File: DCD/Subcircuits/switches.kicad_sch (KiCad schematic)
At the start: 0 parts

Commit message: Did the signal switching, finished ADC, misc changes to top
Decided to go with solder jumpers instead of power switches bc power
switches have no specs of linearity and they would add unnecessary
complexity, development time, and routing problems.

The calibration test has to be done only once and the chamber doesn't
even have to be sealed for it, so it shouldn't add too much hassle.
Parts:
- added C3: 1nF, Capacitor_SMD:C_0603_1608Metric, symbol Device:C_Small
- added JP1, JP2, JP3, JP4, JP9: SolderJumper_3_Bridged12, Jumper:SolderJumper-3_P1.3mm_Bridged12_RoundedPad1.0x1.5mm, symbol Jumper:SolderJumper_3_Bridged12
- added R2, R3, R4, R5, R6, R7: 47, Resistor_SMD:R_0603_1608Metric, symbol Device:R
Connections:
- new net: JP4.1 (A), R6.2, R7.2
- new net: JP1.2 (C), JP4.2 (C)
- new net: JP4.3 (B), R3.2, R4.2
- new net: JP1.1 (A), JP9.1 (A)
- new net: C3.1, JP1.3 (B), R2.1
- new net: JP3.1 (A), JP9.2 (C)
- new net: JP9.3 (B), R2.2
- new net: JP2.1 (A), JP3.2 (C)
- new net: JP3.3 (B), R5.1
- new net ADC1: R4.1
- new net ADC2: R6.1
- new net DAC1: R3.1
- new net DAC2: R7.1
- new net Ext_Analog: JP2.2 (C)
- new net GND: C3.2, JP2.3 (B), R5.2

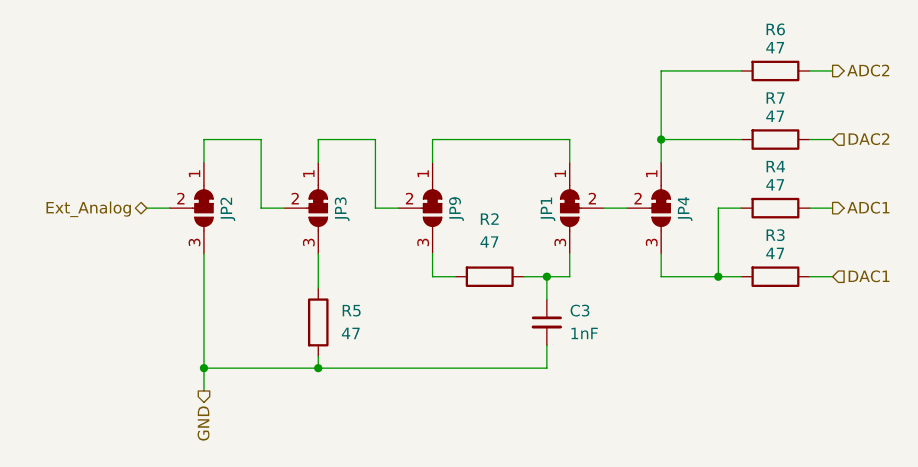
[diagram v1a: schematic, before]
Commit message: Finished switches, added calculations of the current consumption
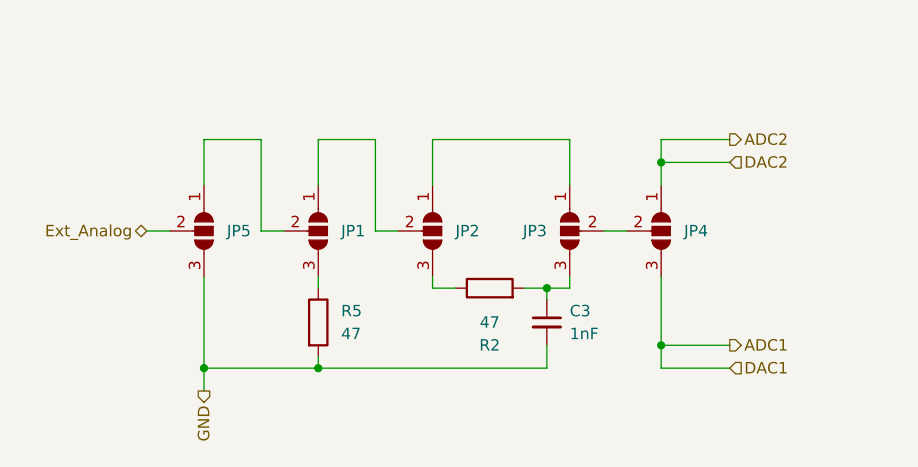
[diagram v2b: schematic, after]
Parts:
- removed JP1, JP2, JP3, JP4, JP9: SolderJumper_3_Bridged12, Jumper:SolderJumper-3_P1.3mm_Bridged12_RoundedPad1.0x1.5mm, symbol Jumper:SolderJumper_3_Bridged12
- removed R3, R4, R6, R7: 47, Resistor_SMD:R_0603_1608Metric, symbol Device:R
- added JP1, JP2, JP3, JP4, JP5: SolderJumper_3_Open, Jumper:SolderJumper-3_P1.3mm_Open_RoundedPad1.0x1.5mm, symbol Jumper:SolderJumper_3_Open
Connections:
- net ADC1: now also JP4.3 (B)
- net ADC2: now also JP4.1 (A)
- net Ext_Analog: now also JP5.2 (C)
- net GND: now also JP5.3 (B)
- net at R2.1: now also JP2.3 (B); no longer C3.1
- net at R2.2: now also C3.1, JP3.3 (B)
- net at R5.1: now also JP1.3 (B)
- new net: JP1.1 (A), JP2.2 (C)
- new net: JP1.2 (C), JP5.1 (A)
- new net: JP2.1 (A), JP3.1 (A)
- new net: JP3.2 (C), JP4.2 (C)
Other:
- moved on the sheet: R2

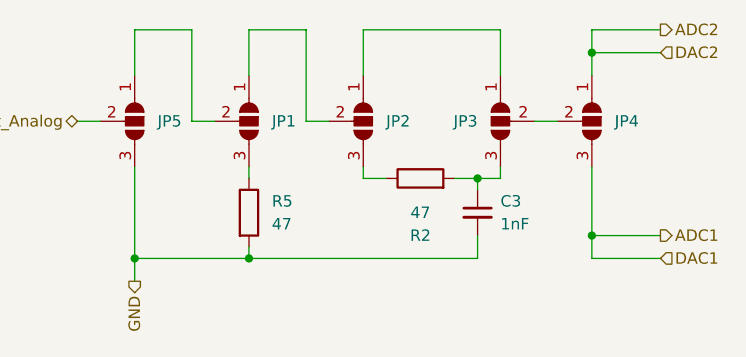
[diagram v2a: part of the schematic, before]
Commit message: Progress on the implementation of the DAC driver
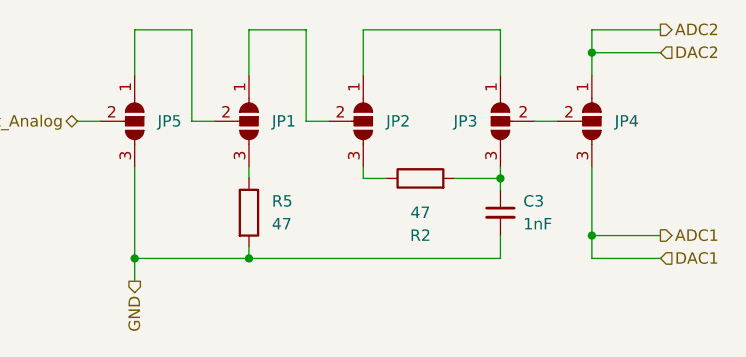
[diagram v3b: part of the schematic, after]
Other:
- moved on the sheet: C3
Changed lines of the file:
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@@
 	(paper "A5")
+	(junction
+		(at 101.6 73.66)
+		(diameter 0)
+		(color 0 0 0 0)
+	)
 	(junction
 		(at 111.76 59.69)
@@
 	)
 	(junction
-		(at 99.06 73.66)
-		(diameter 0)
-		(color 0 0 0 0)
-	)
-	(junction
 		(at 111.76 80.01)
 		(diameter 0)
@@
 	(wire
 		(pts
-			(xy 73.66 82.55) (xy 99.06 82.55)
+			(xy 73.66 82.55) (xy 101.6 82.55)
 		)
 		(stroke
@@
 	(wire
 		(pts
-			(xy 101.6 73.66) (xy 99.06 73.66)
-		)
-		(stroke
-			(width 0)
-			(type default)
-		)
-	)
-	(wire
-		(pts
 			(xy 80.01 57.15) (xy 80.01 67.31)
 		)
@@
 	(wire
 		(pts
-			(xy 99.06 74.93) (xy 99.06 73.66)
-		)
-		(stroke
-			(width 0)
-			(type default)
-		)
-	)
-	(wire
-		(pts
-			(xy 99.06 80.01) (xy 99.06 82.55)
+			(xy 101.6 74.93) (xy 101.6 73.66)
+		)
+		(stroke
+			(width 0)
+			(type default)
+		)
+	)
+	(wire
+		(pts
+			(xy 101.6 80.01) (xy 101.6 82.55)
 		)
 		(stroke
@@
 	(wire
 		(pts
-			(xy 99.06 73.66) (xy 96.52 73.66)
+			(xy 96.52 73.66) (xy 101.6 73.66)
 		)
 		(stroke
@@
 	(symbol
 		(lib_id "Device:C_Small")
-		(at 99.06 77.47 0)
+		(at 101.6 77.47 0)
 		(unit 1)
 		(exclude_from_sim no)
@@
 		(dnp no)
 		(property "Reference" "C3"
-			(at 101.6 76.2 0)
+			(at 104.14 76.2 0)
 			(effects
 				(font
@@
 		)
 		(property "Value" "1nF"
-			(at 101.6 78.74 0)
+			(at 104.14 78.74 0)
 			(effects
 				(font
@@
 		)
 		(property "Footprint" "Capacitor_SMD:C_0603_1608Metric"
-			(at 99.06 77.47 0)
+			(at 101.6 77.47 0)
 			(effects
 				(font
@@
 		)
 		(property "Datasheet" "https://datasheets.kyocera-avx.com/C0GNP0-KGM.pdf"
-			(at 99.06 77.47 0)
+			(at 101.6 77.47 0)
 			(effects
 				(font
@@
 		)
 		(property "Description" ""
-			(at 99.06 77.47 0)
+			(at 101.6 77.47 0)
 			(effects
 				(font
@@
 		)
 		(property "Part number" "0603YA102FAT2A "
-			(at 99.06 77.47 0)
+			(at 101.6 77.47 0)
 			(effects
 				(font
@@
 		)
 		(property "Order number" "581-0603YA102FAT2A"
-			(at 99.06 77.47 0)
+			(at 101.6 77.47 0)
 			(effects
 				(font
@@
 		)
 		(property "Supplier" "Mouser"
-			(at 99.06 77.47 0)
+			(at 101.6 77.47 0)
 			(effects
 				(font
@@
 		)
 		(property "Notes" ""
-			(at 99.06 77.47 0)
+			(at 101.6 77.47 0)
 			(effects
 				(font
@@
 		)
 		(property "Link" "https://www.mouser.com/ProductDetail/KYOCERA-AVX/0603YA102FAT2A?qs=Q0wCMCRSJ1vE1Ym6h4QWAA%3D%3D"
-			(at 99.06 77.47 0)
+			(at 101.6 77.47 0)
 			(effects
 				(font
@@
 		)
 		(property "Mouser No." ""
-			(at 99.06 77.47 0)
-			(effects
-				(font
+			(at 101.6 77.47 0)
+			(effects
+				(font

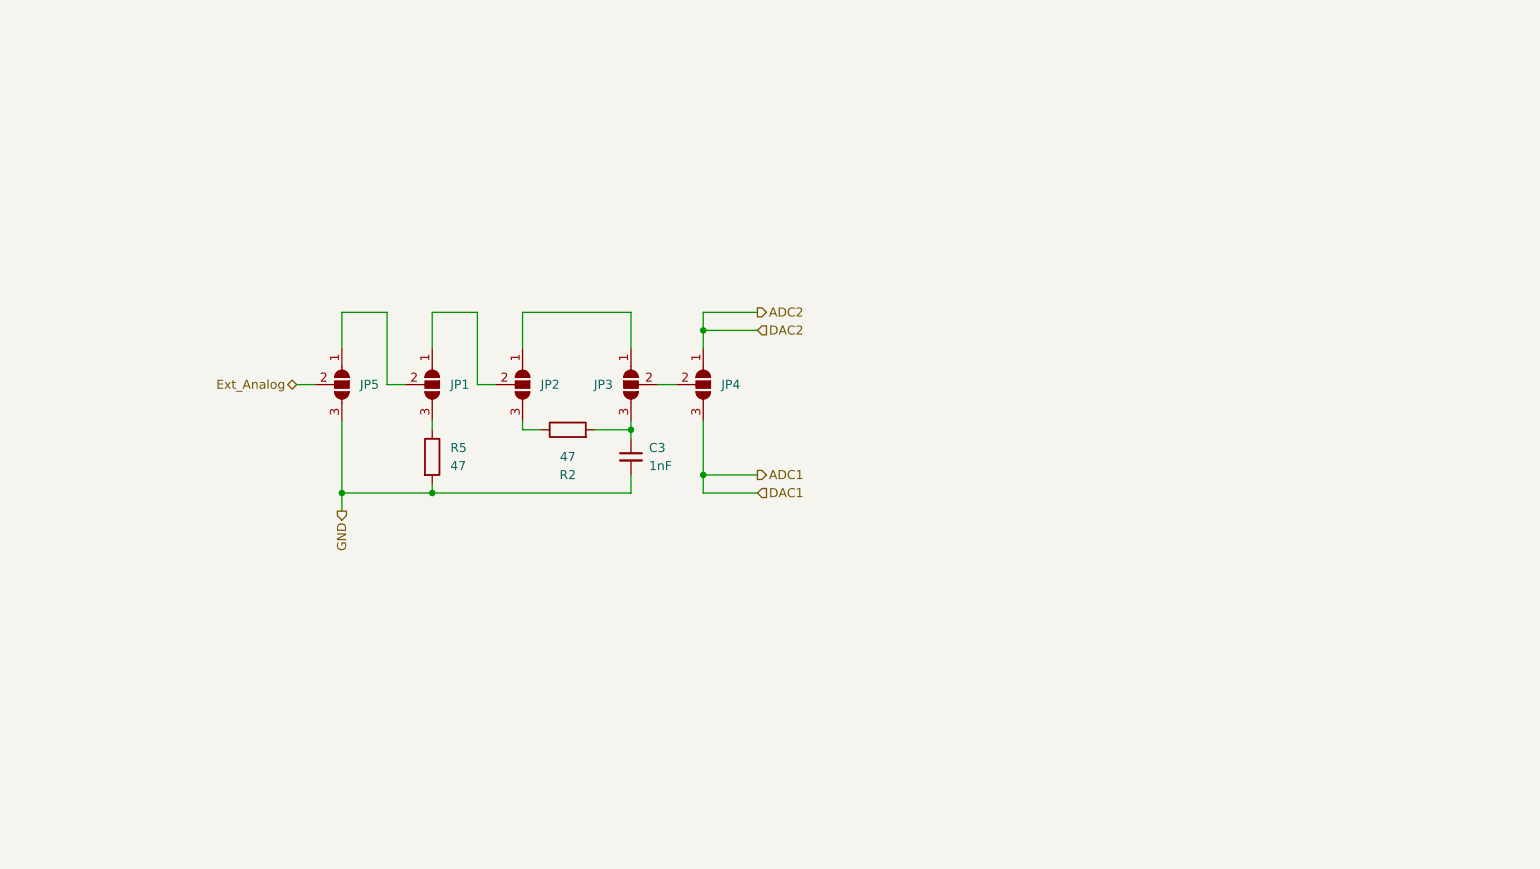
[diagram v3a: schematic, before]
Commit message: Fixed the switches, finished the adc amplifier, missing the filer to adc
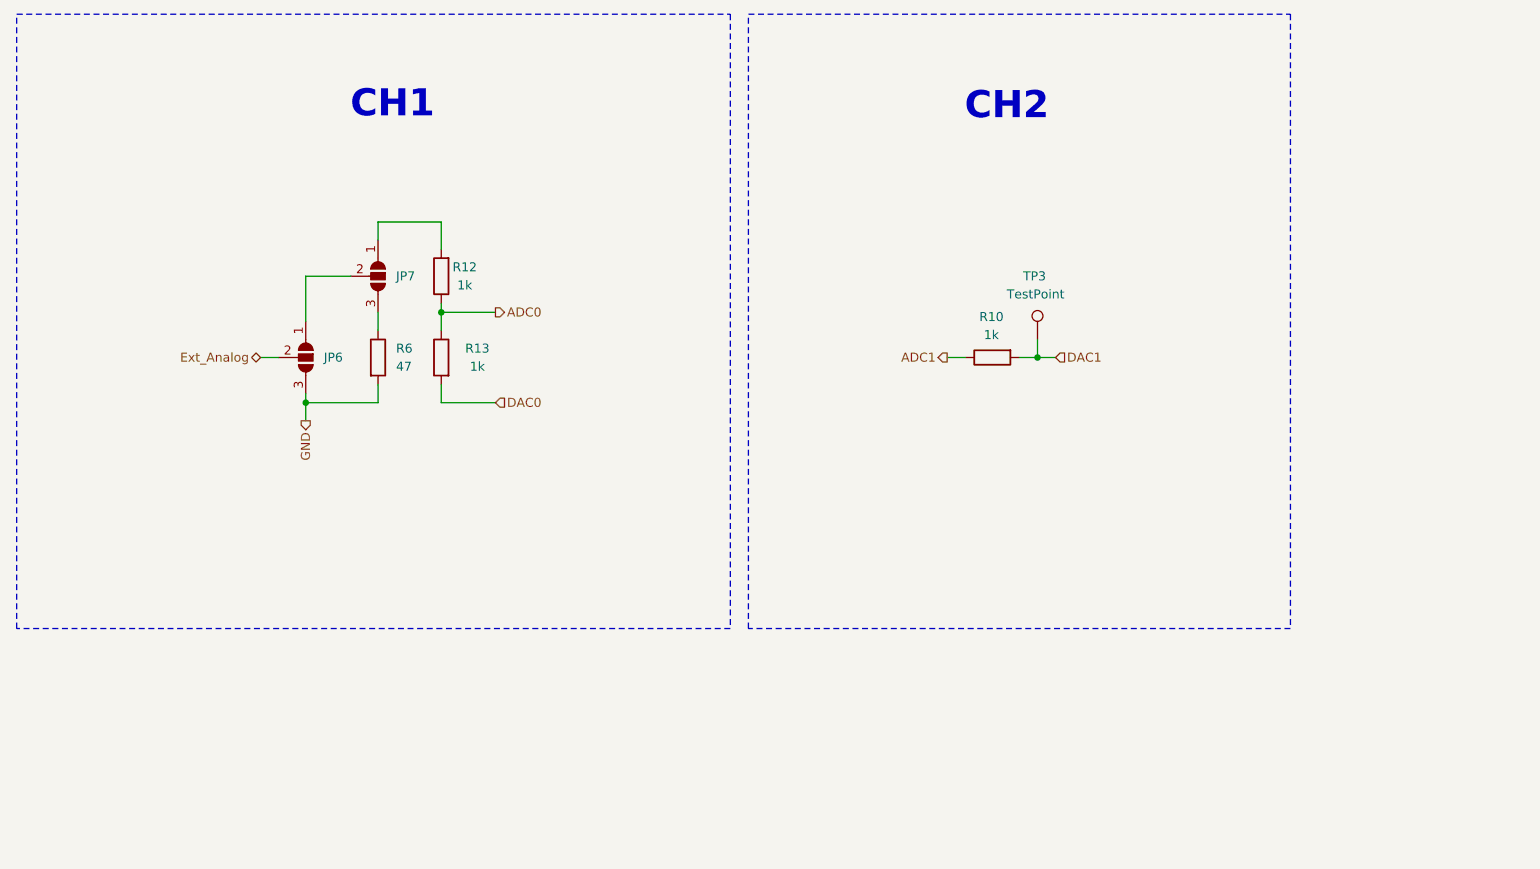
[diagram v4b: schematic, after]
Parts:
- removed C3: 1nF, Capacitor_SMD:C_0603_1608Metric, symbol Device:C_Small
- removed JP1, JP2, JP3, JP4, JP5: SolderJumper_3_Open, Jumper:SolderJumper-3_P1.3mm_Open_RoundedPad1.0x1.5mm, symbol Jumper:SolderJumper_3_Open
- removed R2, R5: 47, Resistor_SMD:R_0603_1608Metric, symbol Device:R
- added JP6, JP7: SolderJumper_3_Open, Jumper:SolderJumper-3_P1.3mm_Open_RoundedPad1.0x1.5mm, symbol Jumper:SolderJumper_3_Open
- added R10, R12, R13: 1k, Resistor_SMD:R_0603_1608Metric, symbol Device:R
- added R6: 47, Resistor_SMD:R_0603_1608Metric, symbol Device:R
- added TP3: TestPoint, TestPoint:TestPoint_Pad_D1.5mm, symbol Connector:TestPoint
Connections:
- net ADC1: now also R10.1
- net Ext_Analog: now also JP6.2 (C)
- net GND: now also JP6.3 (B), R6.2
- new net: JP7.1 (A), R12.2
- new net: JP6.1 (A), JP7.2 (C)
- new net: JP7.3 (B), R6.1
- new net ADC0: R12.1, R13.1
- new net DAC0: R13.2
- new net DAC1: R10.2, TP3.1
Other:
- note added: "CH1"
- note added: "CH2"

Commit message: Finished the schematics. Fixed the comments that we recieved
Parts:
- added JP3: SolderJumper_2_Open, Jumper:SolderJumper-2_P1.3mm_Open_RoundedPad1.0x1.5mm, symbol Jumper:SolderJumper_2_Open
- renumbered JP6 to JP1, JP7 to JP2, R6 to R17, R12 to R18, R13 to R19, R10 to R20
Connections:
- net DAC0: now also JP3.1 (A)
- net at JP2.1 (A), R18.2: now also JP3.2 (B)
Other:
- note added: "Calibration jumpers used to calibrate the transmission line to the chamber. (Can be done without pressurizing the chamber.)"
- note added: "Theory of Operation"
- note added: "Voltage summing node and a jumper to skip it for using the DAC as an external generator and testing the DAC alone."
- moved on the sheet: JP1, JP2, R17, R18, R19, R20, TP3

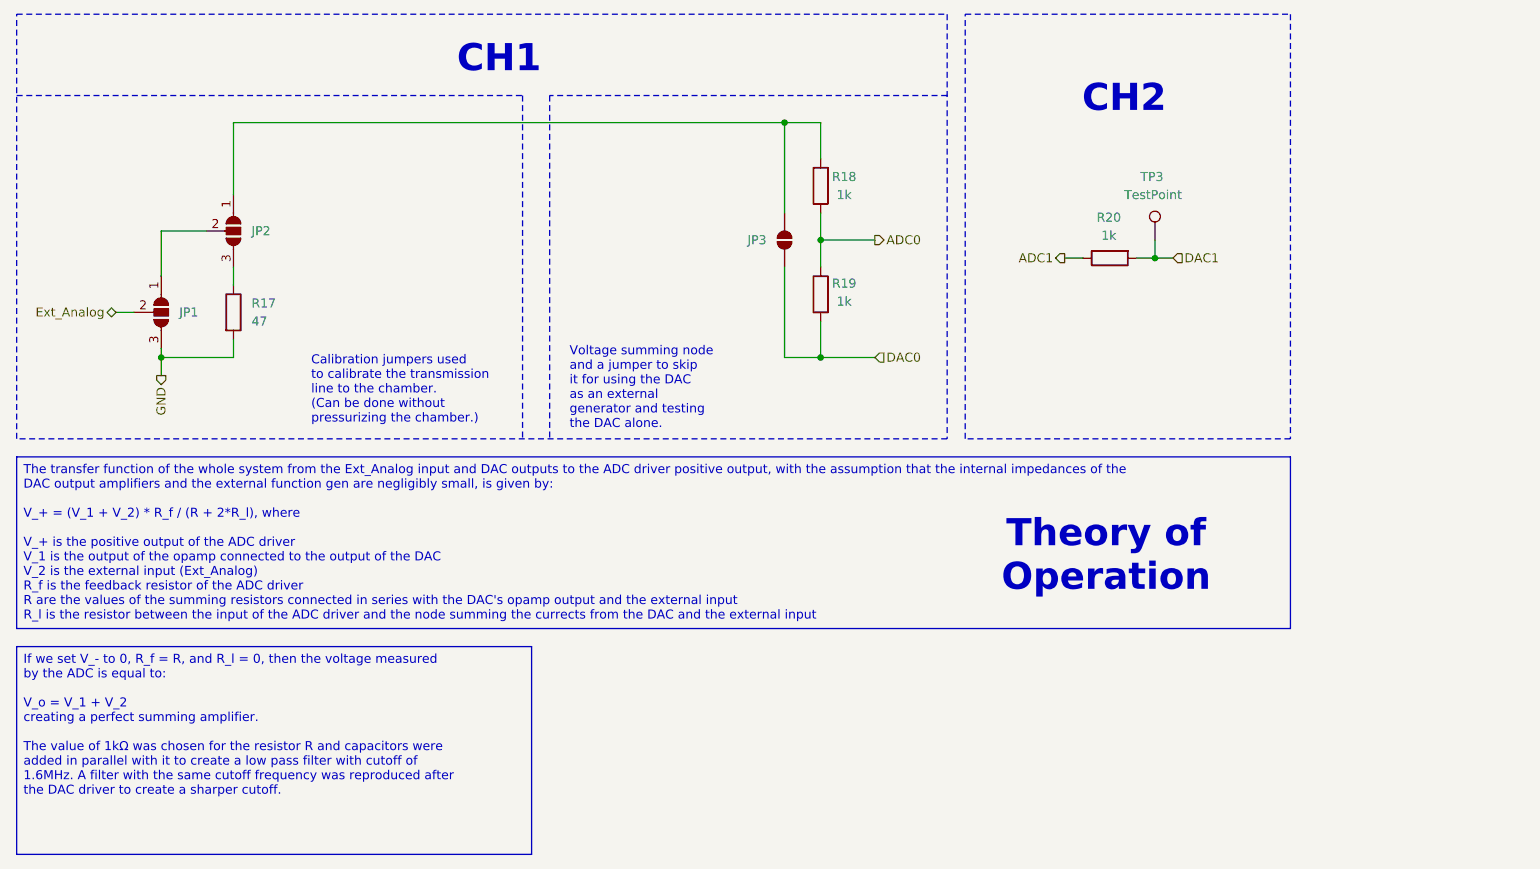
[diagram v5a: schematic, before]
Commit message: Finished
Final touches, PSUs filtering, external connections, psu connections for
the negative voltage, and the DAC higher voltage, and the negative
voltage. Added an external connection directely to the DAC.
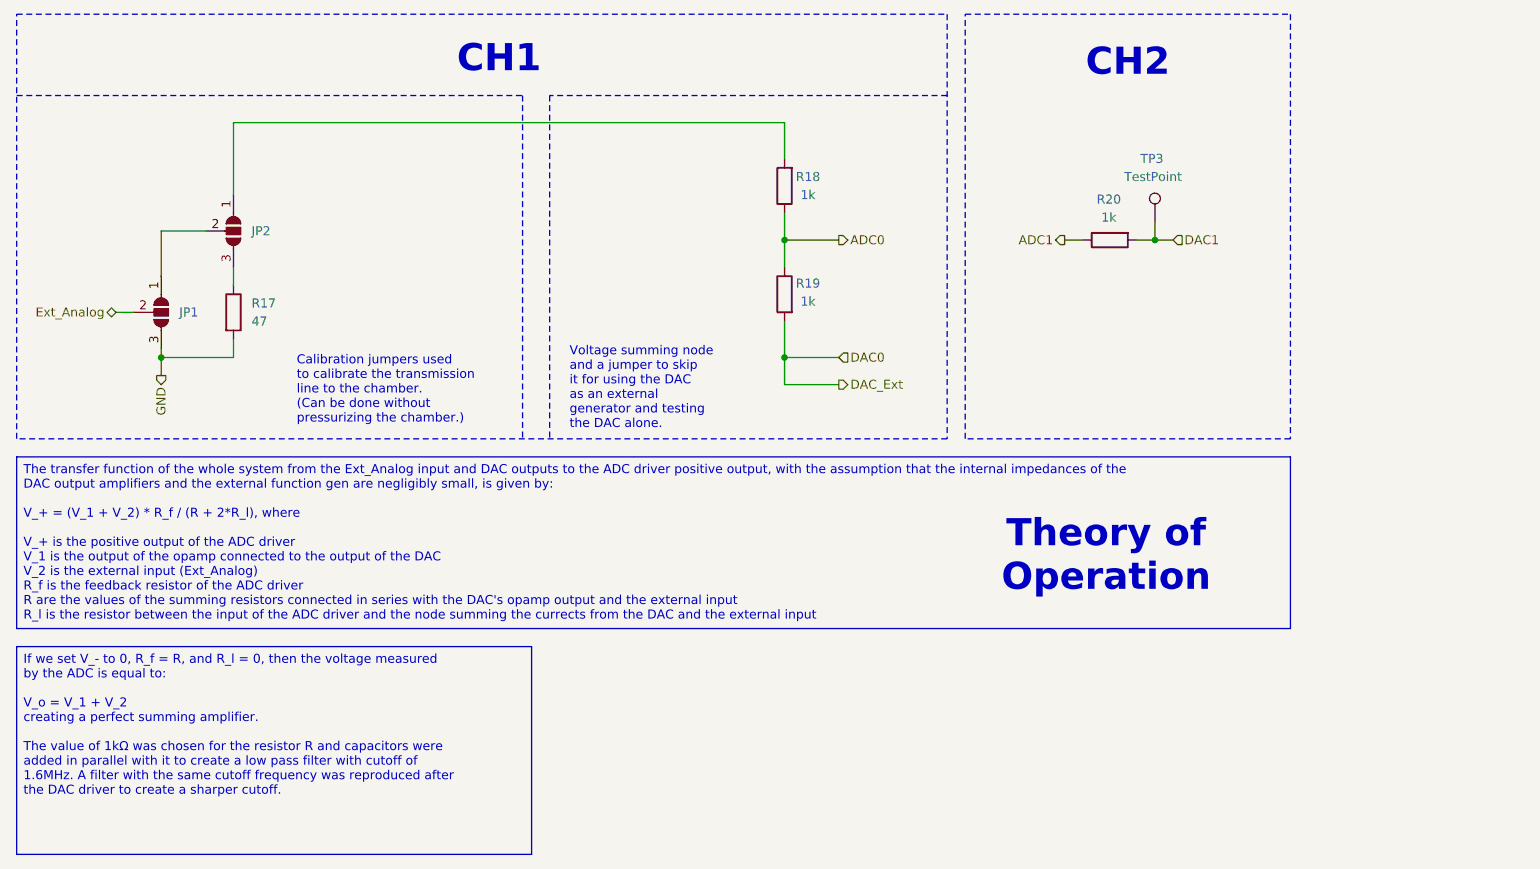
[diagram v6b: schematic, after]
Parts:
- removed JP3: SolderJumper_2_Open, Jumper:SolderJumper-2_P1.3mm_Open_RoundedPad1.0x1.5mm, symbol Jumper:SolderJumper_2_Open
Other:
- moved on the sheet: R18, R19, R20, TP3
